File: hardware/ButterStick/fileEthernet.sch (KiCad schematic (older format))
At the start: 37 parts, among them CON1 JD1_0001NL, U10 XCL206, U11 KSZ9031, U13 SN74LVC1T45, U14 SN74LVC1T45, Y1 25Mhz

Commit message: Routed all SYZYGY ports. Placed decoupling caps etc.
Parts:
- CON1: footprint (none) -> gkl_conn:MAGJACK
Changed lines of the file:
@@
 $Descr A4 11693 8268
 encoding utf-8
-Sheet 6 13
+Sheet 6 14
 Title ""
 Date ""
@@
 F 0 "CON1" H 10282 4346 50  0000 L CNN
 F 1 "JD1_0001NL" H 10282 4255 50  0000 L CNN
-F 2 "" H 9850 5150 50  0001 C CNN
+F 2 "gkl_conn:MAGJACK" H 9850 5150 50  0001 C CNN
 F 3 "" H 9850 5150 50  0001 C CNN
 F 4 "JD1-0001NL" H 0   0   50  0001 C CNN "PN"

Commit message: Added ESD on SD card signals.
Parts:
- C55: footprint Capacitors_SMD:C_0603 -> pkl_dipol:C_0603
- L1: footprint Inductors_SMD:L_0402 -> pkl_dipol:L_0402
- L3: footprint Inductors_SMD:L_0603 -> pkl_dipol:L_0603
- R10, R11, R12, R13, R14, R15, R20, R21, R24, R7, R8, R9: footprint Resistors_SMD:R_0402 -> pkl_dipol:R_0402
- R19: footprint Resistors_SMD:R_0603 -> pkl_dipol:R_0603
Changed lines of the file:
@@
 $Descr A4 11693 8268
 encoding utf-8
-Sheet 6 14
+Sheet 6 13
 Title ""
 Date ""
@@
 F 0 "R19" H 6720 2696 50  0000 L CNN
 F 1 "12.1K" H 6720 2605 50  0000 L CNN
-F 2 "Resistors_SMD:R_0603" V 6580 2650 50  0001 C CNN
+F 2 "pkl_dipol:R_0603" V 6580 2650 50  0001 C CNN
 F 3 "~" H 6650 2650 50  0001 C CNN
 F 4 "P12.0KHCT-ND" H 0   0   50  0001 C CNN "PN"
@@
 F 0 "R7" H 2250 3550 50  0000 L CNN
 F 1 "1k5" H 2250 3450 50  0000 L CNN
-F 2 "Resistors_SMD:R_0402" V 2130 3500 50  0001 C CNN
+F 2 "pkl_dipol:R_0402" V 2130 3500 50  0001 C CNN
 F 3 "~" H 2200 3500 50  0001 C CNN
 F 4 "RC0402FR-071K5L" H 0   0   50  0001 C CNN "PN"
@@
 F 0 "R9" H 2550 3550 50  0000 L CNN
 F 1 "1k5" H 2550 3450 50  0000 L CNN
-F 2 "Resistors_SMD:R_0402" V 2430 3500 50  0001 C CNN
+F 2 "pkl_dipol:R_0402" V 2430 3500 50  0001 C CNN
 F 3 "~" H 2500 3500 50  0001 C CNN
 F 4 "RC0402FR-071K5L" H 0   0   50  0001 C CNN "PN"
@@
 F 0 "R11" H 2850 3550 50  0000 L CNN
 F 1 "1k5" H 2850 3450 50  0000 L CNN
-F 2 "Resistors_SMD:R_0402" V 2730 3500 50  0001 C CNN
+F 2 "pkl_dipol:R_0402" V 2730 3500 50  0001 C CNN
 F 3 "~" H 2800 3500 50  0001 C CNN
 F 4 "RC0402FR-071K5L" H 0   0   50  0001 C CNN "PN"
@@
 F 0 "R13" H 3150 3550 50  0000 L CNN
 F 1 "1k5" H 3150 3450 50  0000 L CNN
-F 2 "Resistors_SMD:R_0402" V 3030 3500 50  0001 C CNN
+F 2 "pkl_dipol:R_0402" V 3030 3500 50  0001 C CNN
 F 3 "~" H 3100 3500 50  0001 C CNN
 F 4 "RC0402FR-071K5L" H 0   0   50  0001 C CNN "PN"
@@
 F 0 "R8" H 2250 5900 50  0000 L CNN
 F 1 "1k5" H 2250 5800 50  0000 L CNN
-F 2 "Resistors_SMD:R_0402" V 2130 5850 50  0001 C CNN
+F 2 "pkl_dipol:R_0402" V 2130 5850 50  0001 C CNN
 F 3 "~" H 2200 5850 50  0001 C CNN
 F 4 "RC0402FR-071K5L" H 0   0   50  0001 C CNN "PN"
@@
 F 0 "R10" H 2550 5900 50  0000 L CNN
 F 1 "1k5" H 2550 5800 50  0000 L CNN
-F 2 "Resistors_SMD:R_0402" V 2430 5850 50  0001 C CNN
+F 2 "pkl_dipol:R_0402" V 2430 5850 50  0001 C CNN
 F 3 "~" H 2500 5850 50  0001 C CNN
 F 4 "RC0402FR-071K5L" H 0   0   50  0001 C CNN "PN"
@@
 F 0 "R12" H 2850 5900 50  0000 L CNN
 F 1 "1k5" H 2850 5800 50  0000 L CNN
-F 2 "Resistors_SMD:R_0402" V 2730 5850 50  0001 C CNN
+F 2 "pkl_dipol:R_0402" V 2730 5850 50  0001 C CNN
 F 3 "~" H 2800 5850 50  0001 C CNN
 F 4 "RC0402FR-071K5L" H 0   0   50  0001 C CNN "PN"
@@
 F 0 "R15" H 6800 4150 50  0000 L CNN
 F 1 "1k5" H 6800 3850 50  0000 L CNN
-F 2 "Resistors_SMD:R_0402" V 6680 4000 50  0001 C CNN
+F 2 "pkl_dipol:R_0402" V 6680 4000 50  0001 C CNN
 F 3 "~" H 6750 4000 50  0001 C CNN
 F 4 "RC0402FR-071K5L" H 0   0   50  0001 C CNN "PN"
@@
 F 0 "R24" H 7100 4150 50  0000 L CNN
 F 1 "1k5" H 7100 3850 50  0000 L CNN
-F 2 "Resistors_SMD:R_0402" V 6980 4000 50  0001 C CNN
+F 2 "pkl_dipol:R_0402" V 6980 4000 50  0001 C CNN
 F 3 "~" H 7050 4000 50  0001 C CNN
 F 4 "RC0402FR-071K5L" H 0   0   50  0001 C CNN "PN"
@@
 F 0 "R14" H 3450 3550 50  0000 L CNN
 F 1 "1k5" H 3450 3450 50  0000 L CNN
-F 2 "Resistors_SMD:R_0402" V 3330 3500 50  0001 C CNN
+F 2 "pkl_dipol:R_0402" V 3330 3500 50  0001 C CNN
 F 3 "~" H 3400 3500 50  0001 C CNN
 F 4 "RC0402FR-071K5L" H 0   0   50  0001 C CNN "PN"
@@
 F 0 "L1" V 2713 2950 50  0000 C CNN
 F 1 "600R" V 2804 2950 50  0000 C CNN
-F 2 "Inductors_SMD:L_0402" V 2880 2950 50  0001 C CNN
+F 2 "pkl_dipol:L_0402" V 2880 2950 50  0001 C CNN
 F 3 "~" H 2950 2950 50  0001 C CNN
 F 4 "490-1006-1-ND" H 0   0   50  0001 C CNN "SN-DK"
@@
 F 0 "L3" V 9313 3400 50  0000 C CNN
 F 1 "600R" V 9404 3400 50  0000 C CNN
-F 2 "Inductors_SMD:L_0603" V 9480 3400 50  0001 C CNN
+F 2 "pkl_dipol:L_0603" V 9480 3400 50  0001 C CNN
 F 3 "~" H 9550 3400 50  0001 C CNN
 F 4 "742792651" H 0   0   50  0001 C CNN "PN"
@@
 F 0 "R21" H 9300 5650 50  0000 L CNN
 F 1 "220R" H 9250 5550 50  0000 L CNN
-F 2 "Resistors_SMD:R_0402" V 9130 5600 50  0001 C CNN
+F 2 "pkl_dipol:R_0402" V 9130 5600 50  0001 C CNN
 F 3 "~" H 9200 5600 50  0001 C CNN
 F 4 "RC0402JR-07220RL" H 0   0   50  0001 C CNN "PN"
@@
 F 0 "R20" H 9200 5550 50  0000 L CNN
 F 1 "220R" H 9150 5650 50  0000 L CNN
-F 2 "Resistors_SMD:R_0402" V 9030 5600 50  0001 C CNN
+F 2 "pkl_dipol:R_0402" V 9030 5600 50  0001 C CNN
 F 3 "~" H 9100 5600 50  0001 C CNN
 F 4 "RC0402JR-07220RL" H 0   0   50  0001 C CNN "PN"
@@
 F 0 "C55" H 3165 1846 50  0000 L CNN
 F 1 "10uF" H 3165 1755 50  0000 L CNN
-F 2 "Capacitors_SMD:C_0603" H 3088 1650 50  0001 C CNN
+F 2 "pkl_dipol:C_0603" H 3088 1650 50  0001 C CNN
 F 3 "~" H 3050 1800 50  0001 C CNN
 F 4 "C1608X5R1A106K080AC" H 0   0   50  0001 C CNN "PN"

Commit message: Update KiCad PCB.
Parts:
- U11: MFG (none) -> Microchip Technology
- Y1: MFG (none) -> Kyocera International Inc. Electronic Components
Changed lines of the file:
@@
 F 4 "KSZ9031RNXCA" H 0   0   50  0001 C CNN "PN"
 F 5 "576-4040-ND" H 0   0   50  0001 C CNN "SN-DK"
+F 6 "Microchip Technology" H 0   0   50  0001 C CNN "MFG"
 	1    5350 3400
 	1    0    0    -1
@@
 F 4 "CX2520DB25000D0FLJC1" H 0   0   50  0001 C CNN "PN"
 F 5 "1253-1723-1-ND" H 0   0   50  0001 C CNN "SN-DK"
+F 6 "Kyocera International Inc. Electronic Components" H 0   0   50  0001 C CNN "MFG"
 	1    7350 1400
 	1    0    0    -1

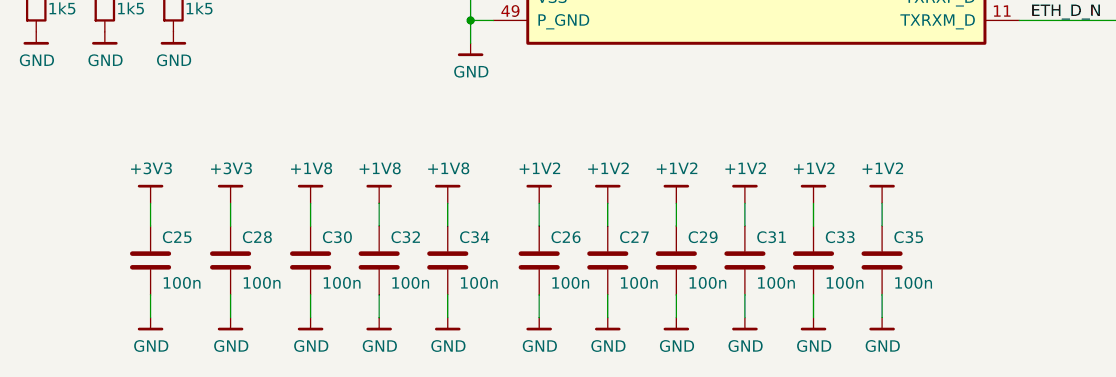
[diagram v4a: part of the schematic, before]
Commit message: Finalised part values update BOM values to reflect. Swapped layers 4/5 due to stackup changes
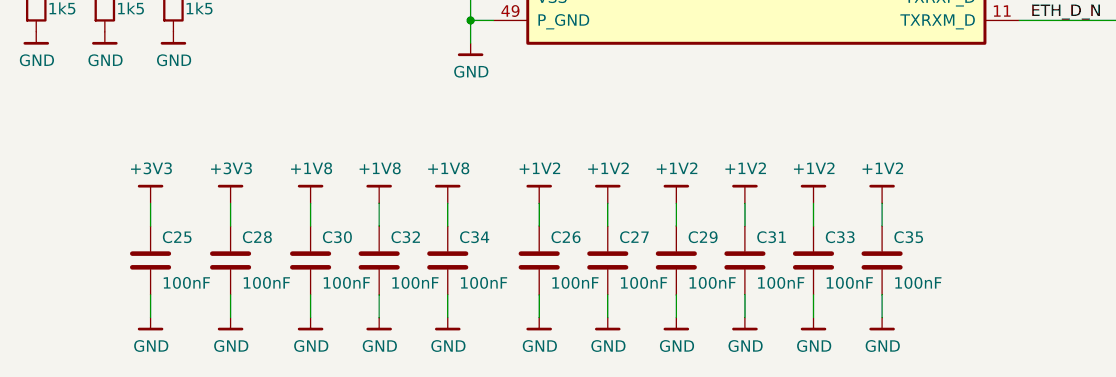
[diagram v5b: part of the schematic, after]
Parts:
- C25, C26, C27, C28, C29, C30, C31, C32, C33, C34, C35: value 100n -> 100nF; Mfg (none) -> Samsung Electro-Mechanics; PN (none) -> CL05B104KP5NNNC
- C36, C37: Mfg (none) -> Samsung Electro-Mechanics; PN (none) -> CL05C220JB5NNWC
- C40, C41: Mfg (none) -> Samsung Electro-Mechanics
- C55: PN C1608X5R1A106K080AC -> CL10A106MP8NNNC
- L1: Mfg (none) -> Samsung Electro-Mechanics; PN (none) -> CIM05U601NC
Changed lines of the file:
@@
 EESchema Schematic File Version 4
 LIBS:ButterStick-cache
-EELAYER 26 0
+EELAYER 29 0
 EELAYER END
 $Descr A4 11693 8268
 encoding utf-8
-Sheet 6 13
-Title ""
-Date ""
-Rev ""
-Comp ""
+Sheet 3 13
+Title "ButterStick"
+Date "2019-03-19"
+Rev "r0_1"
+Comp "GsD"
 Comment1 ""
 Comment2 ""
@@
 F 2 "pkl_dipol:C_0402" H 7138 1000 50  0001 C CNN
 F 3 "~" H 7100 1150 50  0001 C CNN
+F 4 "Samsung Electro-Mechanics" H 0   0   50  0001 C CNN "Mfg"
+F 5 "CL05C220JB5NNWC" H 0   0   50  0001 C CNN "PN"
 	1    7100 1150
 	1    0    0    -1
@@
 F 2 "pkl_dipol:C_0402" H 7638 1000 50  0001 C CNN
 F 3 "~" H 7600 1150 50  0001 C CNN
+F 4 "Samsung Electro-Mechanics" H 0   0   50  0001 C CNN "Mfg"
+F 5 "CL05C220JB5NNWC" H 0   0   50  0001 C CNN "PN"
 	1    7600 1150
 	1    0    0    -1
@@
 P 2700 7000
 F 0 "C25" H 2750 7100 50  0000 L CNN
-F 1 "100n" H 2750 6900 50  0000 L CNN
+F 1 "100nF" H 2750 6900 50  0000 L CNN
 F 2 "pkl_dipol:C_0402" H 2738 6850 50  0001 C CNN
 F 3 "~" H 2700 7000 50  0001 C CNN
+F 4 "Samsung Electro-Mechanics" H 0   0   50  0001 C CNN "Mfg"
+F 5 "CL05B104KP5NNNC" H 0   0   50  0001 C CNN "PN"
 	1    2700 7000
 	1    0    0    -1
@@
 P 3050 7000
 F 0 "C28" H 3100 7100 50  0000 L CNN
-F 1 "100n" H 3100 6900 50  0000 L CNN
+F 1 "100nF" H 3100 6900 50  0000 L CNN
 F 2 "pkl_dipol:C_0402" H 3088 6850 50  0001 C CNN
 F 3 "~" H 3050 7000 50  0001 C CNN
+F 4 "Samsung Electro-Mechanics" H 0   0   50  0001 C CNN "Mfg"
+F 5 "CL05B104KP5NNNC" H 0   0   50  0001 C CNN "PN"
 	1    3050 7000
 	1    0    0    -1
@@
 P 3400 7000
 F 0 "C30" H 3450 7100 50  0000 L CNN
-F 1 "100n" H 3450 6900 50  0000 L CNN
+F 1 "100nF" H 3450 6900 50  0000 L CNN
 F 2 "pkl_dipol:C_0402" H 3438 6850 50  0001 C CNN
 F 3 "~" H 3400 7000 50  0001 C CNN
+F 4 "Samsung Electro-Mechanics" H 0   0   50  0001 C CNN "Mfg"
+F 5 "CL05B104KP5NNNC" H 0   0   50  0001 C CNN "PN"
 	1    3400 7000
 	1    0    0    -1
@@
 P 3700 7000
 F 0 "C32" H 3750 7100 50  0000 L CNN
-F 1 "100n" H 3750 6900 50  0000 L CNN
+F 1 "100nF" H 3750 6900 50  0000 L CNN
 F 2 "pkl_dipol:C_0402" H 3738 6850 50  0001 C CNN
 F 3 "~" H 3700 7000 50  0001 C CNN
+F 4 "Samsung Electro-Mechanics" H 0   0   50  0001 C CNN "Mfg"
+F 5 "CL05B104KP5NNNC" H 0   0   50  0001 C CNN "PN"
 	1    3700 7000
 	1    0    0    -1
@@
 P 4000 7000
 F 0 "C34" H 4050 7100 50  0000 L CNN
-F 1 "100n" H 4050 6900 50  0000 L CNN
+F 1 "100nF" H 4050 6900 50  0000 L CNN
 F 2 "pkl_dipol:C_0402" H 4038 6850 50  0001 C CNN
 F 3 "~" H 4000 7000 50  0001 C CNN
+F 4 "Samsung Electro-Mechanics" H 0   0   50  0001 C CNN "Mfg"
+F 5 "CL05B104KP5NNNC" H 0   0   50  0001 C CNN "PN"
 	1    4000 7000
 	1    0    0    -1
@@
 P 4400 7000
 F 0 "C26" H 4450 7100 50  0000 L CNN
-F 1 "100n" H 4450 6900 50  0000 L CNN
+F 1 "100nF" H 4450 6900 50  0000 L CNN
 F 2 "pkl_dipol:C_0402" H 4438 6850 50  0001 C CNN
 F 3 "~" H 4400 7000 50  0001 C CNN
+F 4 "Samsung Electro-Mechanics" H 0   0   50  0001 C CNN "Mfg"
+F 5 "CL05B104KP5NNNC" H 0   0   50  0001 C CNN "PN"
 	1    4400 7000
 	1    0    0    -1
@@
 P 4700 7000
 F 0 "C27" H 4750 7100 50  0000 L CNN
-F 1 "100n" H 4750 6900 50  0000 L CNN
+F 1 "100nF" H 4750 6900 50  0000 L CNN
 F 2 "pkl_dipol:C_0402" H 4738 6850 50  0001 C CNN
 F 3 "~" H 4700 7000 50  0001 C CNN
+F 4 "Samsung Electro-Mechanics" H 0   0   50  0001 C CNN "Mfg"
+F 5 "CL05B104KP5NNNC" H 0   0   50  0001 C CNN "PN"
 	1    4700 7000
 	1    0    0    -1
@@
 P 5000 7000
 F 0 "C29" H 5050 7100 50  0000 L CNN
-F 1 "100n" H 5050 6900 50  0000 L CNN
+F 1 "100nF" H 5050 6900 50  0000 L CNN
 F 2 "pkl_dipol:C_0402" H 5038 6850 50  0001 C CNN
 F 3 "~" H 5000 7000 50  0001 C CNN
+F 4 "Samsung Electro-Mechanics" H 0   0   50  0001 C CNN "Mfg"
+F 5 "CL05B104KP5NNNC" H 0   0   50  0001 C CNN "PN"
 	1    5000 7000
 	1    0    0    -1
@@
 P 5300 7000
 F 0 "C31" H 5350 7100 50  0000 L CNN
-F 1 "100n" H 5350 6900 50  0000 L CNN
+F 1 "100nF" H 5350 6900 50  0000 L CNN
 F 2 "pkl_dipol:C_0402" H 5338 6850 50  0001 C CNN
 F 3 "~" H 5300 7000 50  0001 C CNN
+F 4 "Samsung Electro-Mechanics" H 0   0   50  0001 C CNN "Mfg"
+F 5 "CL05B104KP5NNNC" H 0   0   50  0001 C CNN "PN"
 	1    5300 7000
 	1    0    0    -1
@@
 P 5600 7000
 F 0 "C33" H 5650 7100 50  0000 L CNN
-F 1 "100n" H 5650 6900 50  0000 L CNN
+F 1 "100nF" H 5650 6900 50  0000 L CNN
 F 2 "pkl_dipol:C_0402" H 5638 6850 50  0001 C CNN
 F 3 "~" H 5600 7000 50  0001 C CNN
+F 4 "Samsung Electro-Mechanics" H 0   0   50  0001 C CNN "Mfg"
+F 5 "CL05B104KP5NNNC" H 0   0   50  0001 C CNN "PN"
 	1    5600 7000
 	1    0    0    -1
@@
 P 5900 7000
 F 0 "C35" H 5950 7100 50  0000 L CNN
-F 1 "100n" H 5950 6900 50  0000 L CNN
+F 1 "100nF" H 5950 6900 50  0000 L CNN
 F 2 "pkl_dipol:C_0402" H 5938 6850 50  0001 C CNN
 F 3 "~" H 5900 7000 50  0001 C CNN
+F 4 "Samsung Electro-Mechanics" H 0   0   50  0001 C CNN "Mfg"
+F 5 "CL05B104KP5NNNC" H 0   0   50  0001 C CNN "PN"
 	1    5900 7000
 	1    0    0    -1
@@
 F 3 "~" H 2950 2950 50  0001 C CNN
 F 4 "490-1006-1-ND" H 0   0   50  0001 C CNN "SN-DK"
+F 5 "Samsung Electro-Mechanics" H 0   0   50  0001 C CNN "Mfg"
+F 6 "CIM05U601NC" H 0   0   50  0001 C CNN "PN"
 	1    2950 2950
 	0    1    1    0
@@
 F 4 "CL10A475KP8NNNC" H 0   0   50  0001 C CNN "PN"
 F 5 "1276-1044-1-ND" H 0   0   50  0001 C CNN "SN-DK"
+F 6 "Samsung Electro-Mechanics" H 0   0   50  0001 C CNN "Mfg"
 	1    3300 2700
 	1    0    0    -1
@@
 F 4 "CL10A475KP8NNNC" H 0   0   50  0001 C CNN "PN"
 F 5 "1276-1044-1-ND" H 0   0   50  0001 C CNN "SN-DK"
+F 6 "Samsung Electro-Mechanics" H 0   0   50  0001 C CNN "Mfg"
 	1    1050 1350
 	1    0    0    -1
@@
 F 2 "pkl_dipol:C_0603" H 3088 1650 50  0001 C CNN
 F 3 "~" H 3050 1800 50  0001 C CNN
-F 4 "C1608X5R1A106K080AC" H 0   0   50  0001 C CNN "PN"
-F 5 "445-7486-1-ND" H 0   0   50  0001 C CNN "SN-DK"
+F 4 "445-7486-1-ND" H 0   0   50  0001 C CNN "SN-DK"
+F 5 "CL10A106MP8NNNC" H 0   0   50  0001 C CNN "PN"
 	1    3050 1800
 	1    0    0    -1
